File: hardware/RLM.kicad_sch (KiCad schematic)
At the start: 28 parts, among them J1 Conn_01x03, J2 Conn_01x03, SW1 SW_Push, SW2 SW_Push, U3 AP1117-33, U7 MCP2562-E-SN

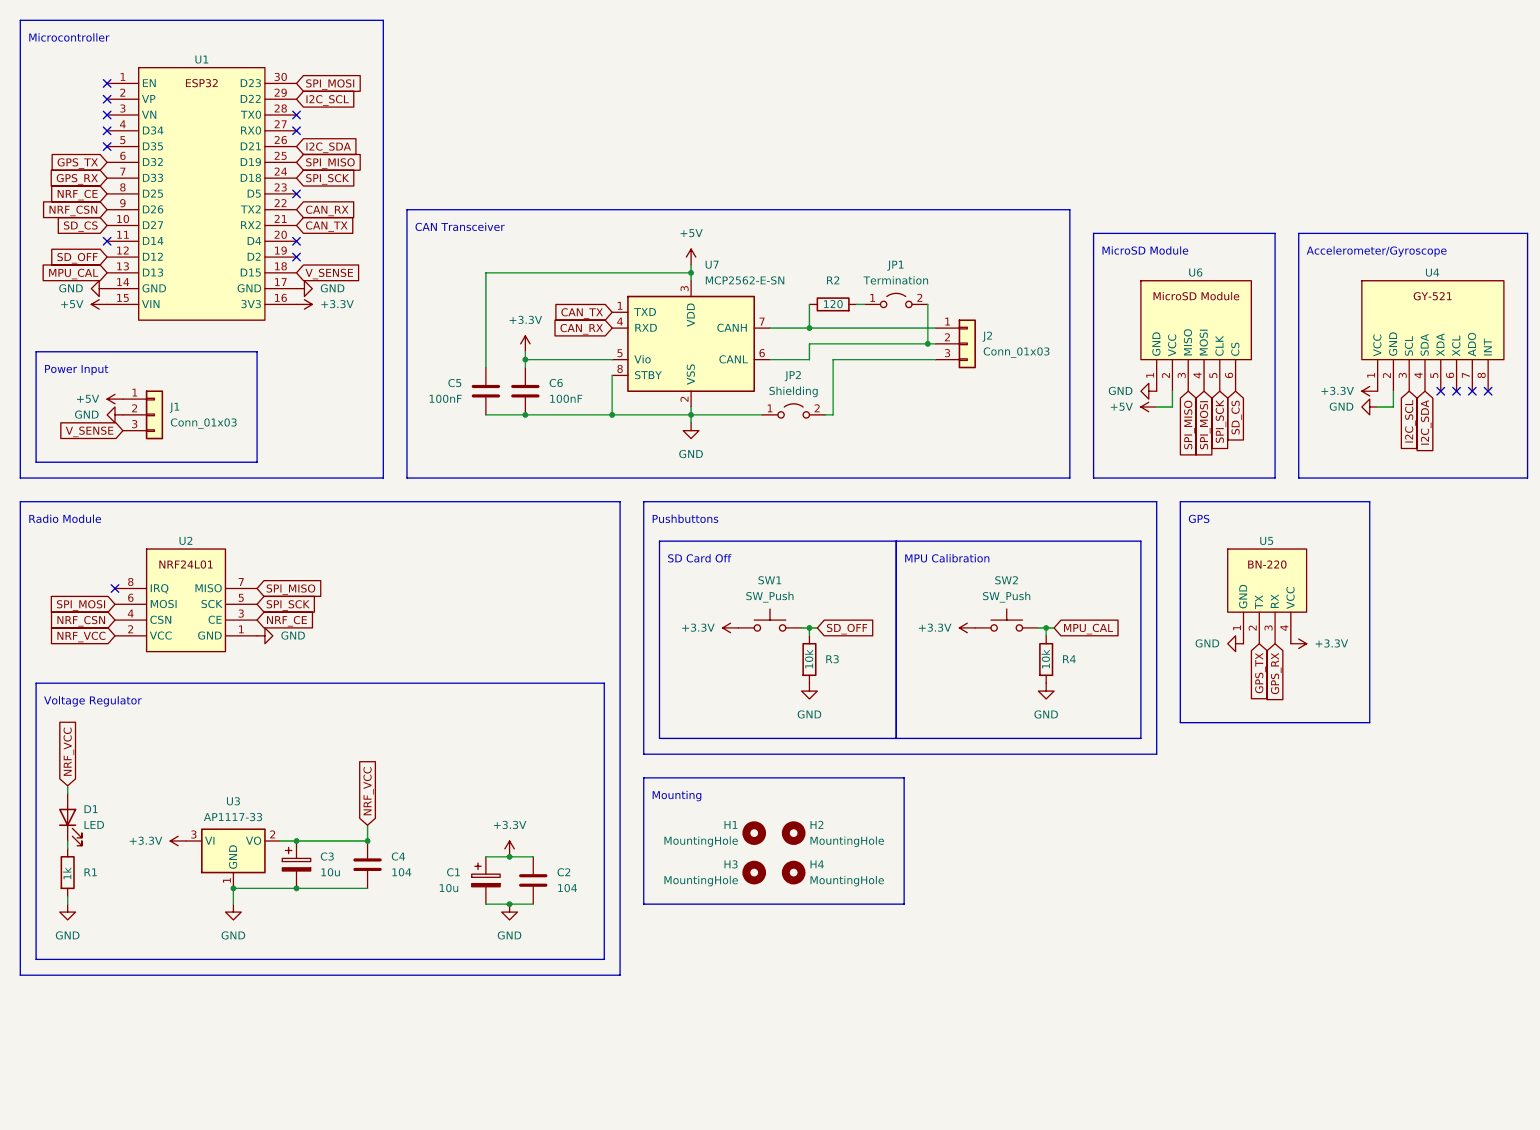
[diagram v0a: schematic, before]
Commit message: feat: update symbols to have VCC up and GND down
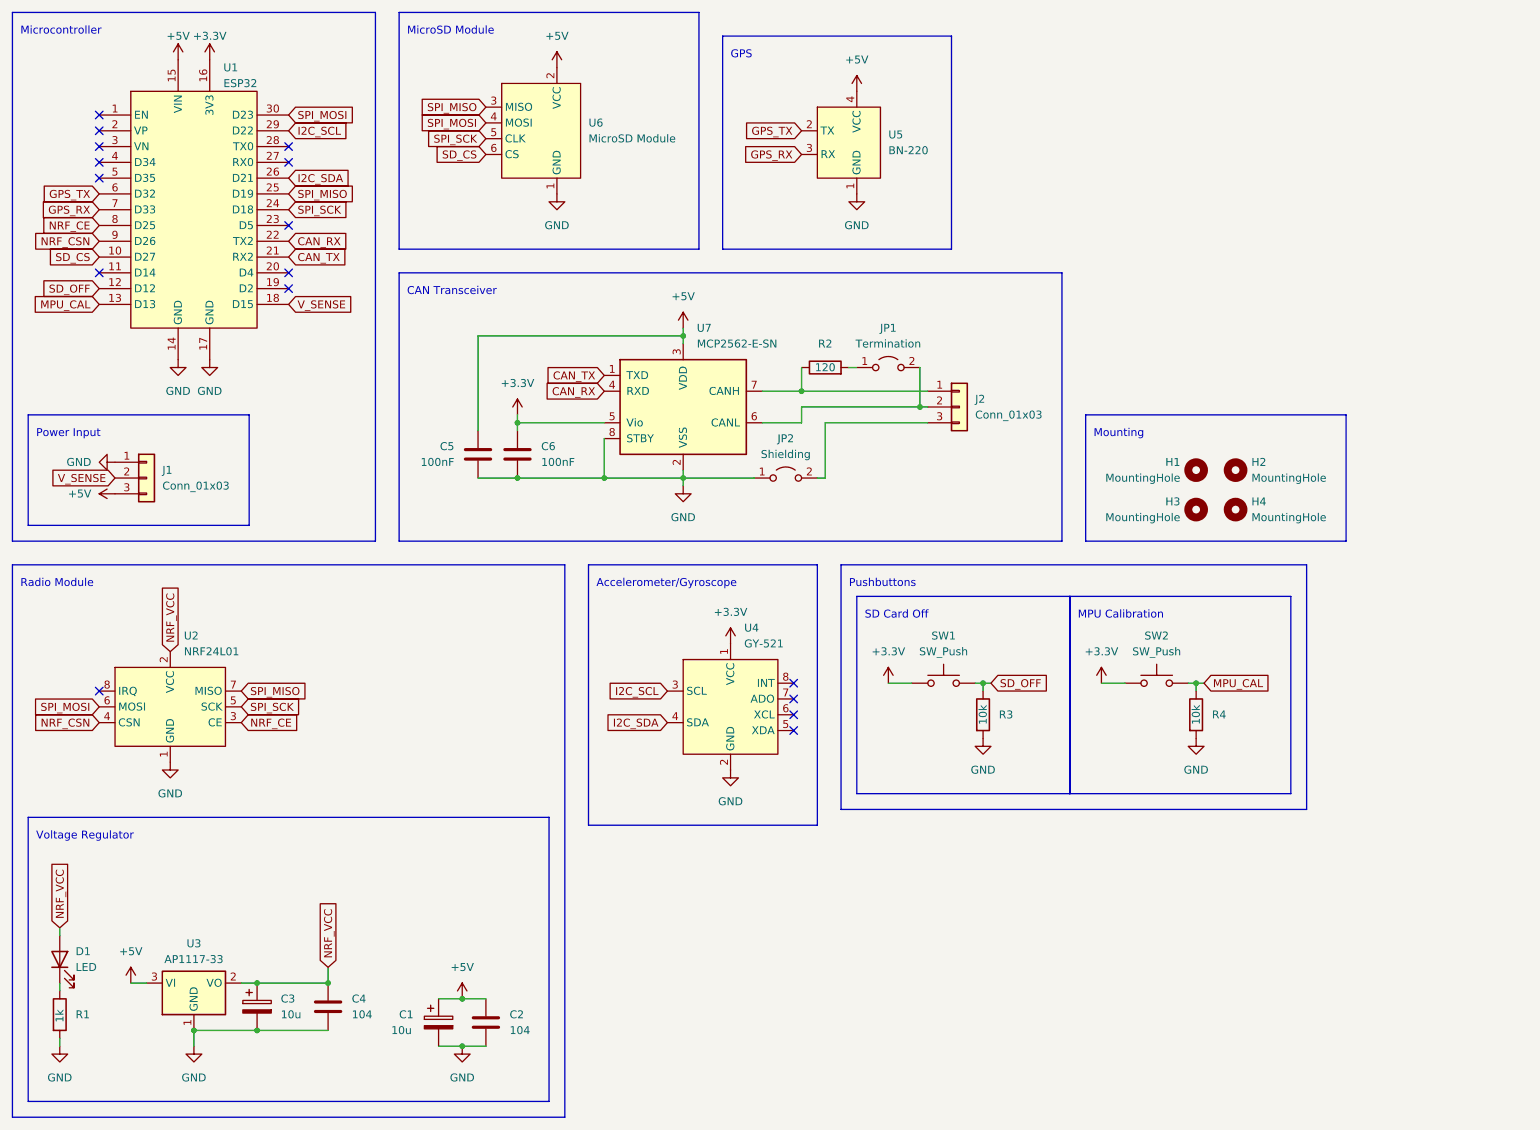
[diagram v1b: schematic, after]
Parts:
- U1: value ~ -> ESP32
- U2: value ~ -> NRF24L01
- U4: value ~ -> GY-521
- U5: value ~ -> BN-220
- U6: value ~ -> MicroSD Module
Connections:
- net +3.3V: no longer C1.1, C2.1, U3.3 (VI), U5.4 (VCC)
- net +5V: now also C1.1, C2.1, J1.3 (Pin_3), U3.3 (VI), U5.4 (VCC); no longer J1.1 (Pin_1)
- net GND: now also J1.1 (Pin_1); no longer J1.2 (Pin_2)
- net V_SENSE: now also J1.2 (Pin_2); no longer J1.3 (Pin_3)
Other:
- moved on the sheet: C1, C2, C3, C4, C5, C6, D1, H1, H2, H3, H4, J1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

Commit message: feat: trace board
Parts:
- C2, C4: value 104 -> 1u
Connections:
- net +3.3V: no longer U4.1 (VCC)
- net +5V: now also U4.1 (VCC)
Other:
- note added: "Note: I2C pullup resistors (4.7k) are on the module"
- moved on the sheet: R3, R4, SW1, SW2

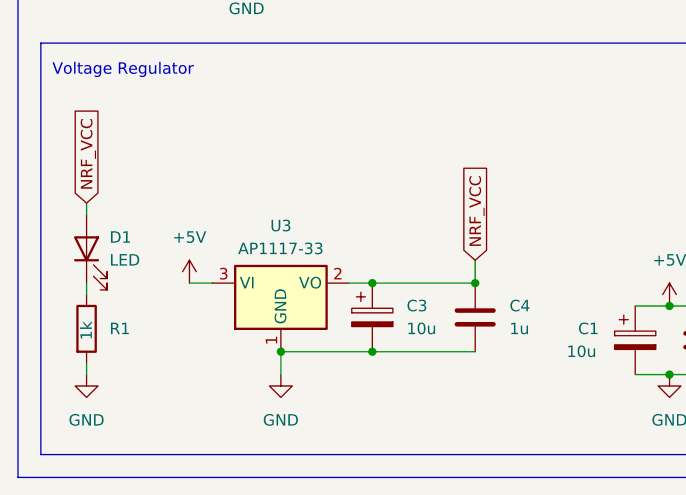
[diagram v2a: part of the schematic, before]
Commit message: fix: CAN resistances, ground pour, logo
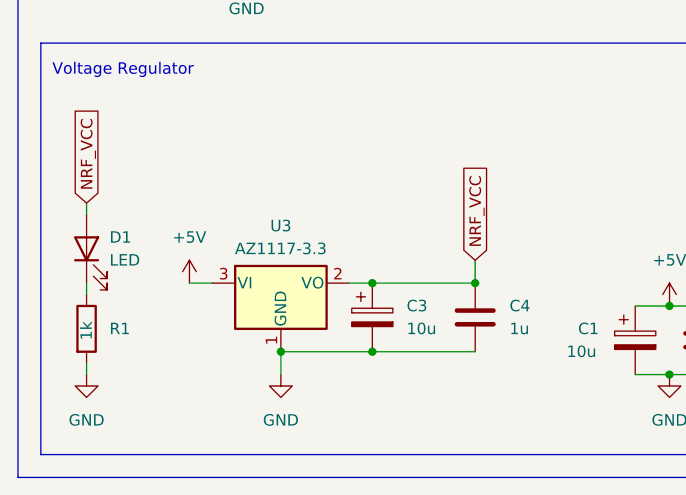
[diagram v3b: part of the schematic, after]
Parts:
- removed U3: AP1117-33, Package_TO_SOT_SMD:SOT-223-3_TabPin2, symbol Regulator_Linear:AP1117-33
- added U3: AZ1117-3.3, symbol Regulator_Linear:AZ1117-3.3
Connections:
- net +5V: now also U3.3 (VI)
- net GND: now also U3.1 (GND)
- net NRF_VCC: now also U3.2 (VO)
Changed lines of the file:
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@@
   (junction (at 97.79 82.55) (diameter 0) (color 0 0 0 0)
   )
+  (junction (at 124.46 91.44) (diameter 0) (color 0 0 0 0)
+  )
+  (junction (at 55.88 180.34) (diameter 0) (color 0 0 0 0)
+  )
+  (junction (at 189.23 124.46) (diameter 0) (color 0 0 0 0)
+  )
+  (junction (at 162.56 80.01) (diameter 0) (color 0 0 0 0)
+  )
+  (junction (at 55.88 172.72) (diameter 0) (color 0 0 0 0)
+  )
   (junction (at 45.72 180.34) (diameter 0) (color 0 0 0 0)
-  )
-  (junction (at 124.46 91.44) (diameter 0) (color 0 0 0 0)
-  )
-  (junction (at 55.88 180.34) (diameter 0) (color 0 0 0 0)
-  )
-  (junction (at 189.23 124.46) (diameter 0) (color 0 0 0 0)
-  )
-  (junction (at 162.56 80.01) (diameter 0) (color 0 0 0 0)
-  )
-  (junction (at 55.88 172.72) (diameter 0) (color 0 0 0 0)
   )
   (junction (at 111.76 91.44) (diameter 0) (color 0 0 0 0)
@@
     )
   )
+  (symbol (lib_id "Regulator_Linear:AZ1117-3.3") (at 45.72 172.72 0) (unit 1)
+    (in_bom yes) (on_board yes) (dnp no) (fields_autoplaced)
+    (property "Reference" "U3" (at 45.72 166.37 0)
+      (effects (font (size 1.27 1.27)))
+    )
+    (property "Value" "AZ1117-3.3" (at 45.72 168.91 0)
+      (effects (font (size 1.27 1.27)))
+    )
+    (property "Footprint" "" (at 45.72 166.37 0)
+      (effects (font (size 1.27 1.27) italic) hide)
+    )
+    (property "Datasheet" "https://www.diodes.com/assets/Datasheets/AZ1117.pdf" (at 45.72 172.72 0)
+      (effects (font (size 1.27 1.27)) hide)
+    )
+    (pin "3")
+    (pin "1")
+    (pin "2")
+    (instances
+      (project "RLM"
+        (path "/3fe8a1ac-6190-4220-82eb-f4588302947e"
+          (reference "U3") (unit 1)
+        )
+      )
+    )
+  )
   (symbol (lib_id "power:+3.3V") (at 48.26 24.13 0) (unit 1)
     (in_bom yes) (on_board yes) (dnp no) (fields_autoplaced)
@@
         )
       )
-    )
-  )
-  (symbol (lib_id "Regulator_Linear:AP1117-33") (at 45.72 172.72 0) (unit 1)
-    (in_bom yes) (on_board yes) (dnp no) (fields_autoplaced)
-    (property "Reference" "U3" (at 45.72 166.37 0)
-      (effects (font (size 1.27 1.27)))
-    )
-    (property "Value" "AP1117-33" (at 45.72 168.91 0)
-      (effects (font (size 1.27 1.27)))
-    )
-    (property "Footprint" "Package_TO_SOT_SMD:SOT-223-3_TabPin2" (at 45.72 167.64 0)
-      (effects (font (size 1.27 1.27)) hide)
-    )
-    (property "Datasheet" "http://www.diodes.com/datasheets/AP1117.pdf" (at 48.26 179.07 0)
-      (effects (font (size 1.27 1.27)) hide)
-    )
-    (pin "1")
-    (pin "2")
-    (pin "3")
-    (instances
-      (project "RLM"
-        (path "/3fe8a1ac-6190-4220-82eb-f4588302947e"
-          (reference "U3") (unit 1)
-        )
-      )
